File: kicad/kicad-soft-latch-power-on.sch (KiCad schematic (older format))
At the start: 9 parts, among them J1 Conn_01x03, J2 Conn_01x03, Q1 SI9942DY, SW1 SW_Push

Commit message: pcb update
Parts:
- added V?: VDC, symbol Simulation_SPICE:VDC
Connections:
- net GND: now also V?.2
- net V_IN: now also V?.1
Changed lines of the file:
@@
 Wire Wire Line
 	6900 3300 7100 3300
+Text GLabel 4550 2550 1    50   Input ~ 0
+V_IN
+$Comp
+L Simulation_SPICE:VDC V?
+U 1 1 61A0B573
+P 4550 2800
+F 0 "V?" H 4680 2891 50  0000 L CNN
+F 1 "VDC" H 4680 2800 50  0000 L CNN
+F 2 "" H 4550 2800 50  0001 C CNN
+F 3 "~" H 4550 2800 50  0001 C CNN
+F 4 "Y" H 4550 2800 50  0001 L CNN "Spice_Netlist_Enabled"
+F 5 "V" H 4550 2800 50  0001 L CNN "Spice_Primitive"
+F 6 "dc(1)" H 4680 2709 50  0000 L CNN "Spice_Model"
+	1    4550 2800
+	1    0    0    -1
+$EndComp
+Wire Wire Line
+	4550 2550 4550 2600
+$Comp
+L power:GND #PWR?
+U 1 1 61A0D8FF
+P 4550 3050
+F 0 "#PWR?" H 4550 2800 50  0001 C CNN
+F 1 "GND" H 4700 3050 50  0000 C CNN
+F 2 "" H 4550 3050 50  0001 C CNN
+F 3 "" H 4550 3050 50  0001 C CNN
+	1    4550 3050
+	1    0    0    -1
+$EndComp
+Wire Wire Line
+	4550 3050 4550 3000
 $EndSCHEMATC

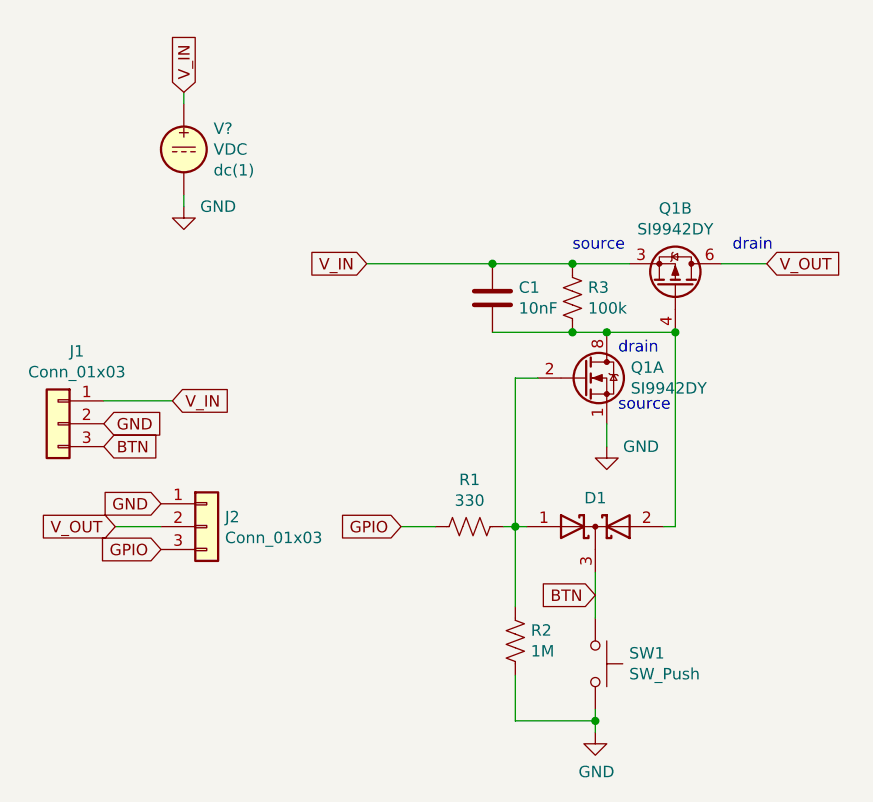
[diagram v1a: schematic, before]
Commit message: add reverse polarity protection
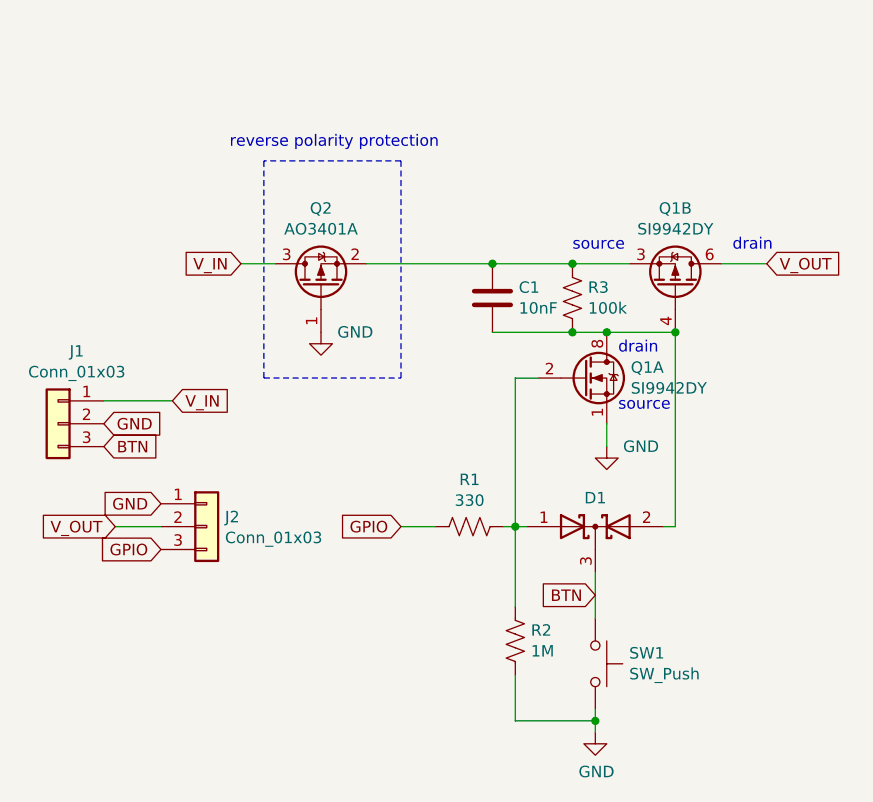
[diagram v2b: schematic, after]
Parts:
- removed V?: VDC, symbol Simulation_SPICE:VDC
- added Q2: AO3401A, Package_TO_SOT_SMD:SOT-23, symbol Transistor_FET:AO3401A
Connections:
- net GND: now also Q2.1 (G)
- net V_IN: now also Q2.3 (D); no longer C1.1, Q1.3 (1), R3.1
- new net: C1.1, Q1.3 (1), Q2.2 (S), R3.1
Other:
- note added: "reverse polarity protection"
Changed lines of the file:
@@
 Text GLabel 7100 3300 2    50   Input ~ 0
 V_OUT
-Text GLabel 5350 3300 0    50   Input ~ 0
+Text GLabel 4800 3300 0    50   Input ~ 0
 V_IN
 Wire Wire Line
@@
 Wire Wire Line
 	6900 3300 7100 3300
-Text GLabel 4550 2550 1    50   Input ~ 0
-V_IN
 $Comp
-L Simulation_SPICE:VDC V?
-U 1 1 61A0B573
-P 4550 2800
-F 0 "V?" H 4680 2891 50  0000 L CNN
-F 1 "VDC" H 4680 2800 50  0000 L CNN
-F 2 "" H 4550 2800 50  0001 C CNN
-F 3 "~" H 4550 2800 50  0001 C CNN
-F 4 "Y" H 4550 2800 50  0001 L CNN "Spice_Netlist_Enabled"
-F 5 "V" H 4550 2800 50  0001 L CNN "Spice_Primitive"
-F 6 "dc(1)" H 4680 2709 50  0000 L CNN "Spice_Model"
-	1    4550 2800
+L Transistor_FET:AO3401A Q2
+U 1 1 61A98F12
+P 5150 3400
+F 0 "Q2" V 5492 3400 50  0000 C CNN
+F 1 "AO3401A" V 5401 3400 50  0000 C CNN
+F 2 "Package_TO_SOT_SMD:SOT-23" H 5350 3325 50  0001 L CIN
+F 3 "http://www.aosmd.com/pdfs/datasheet/AO3401A.pdf" H 5150 3400 50  0001 L CNN
+	1    5150 3400
+	0    -1   -1   0
+$EndComp
+$Comp
+L power:GND #PWR04
+U 1 1 61A9DB9F
+P 5150 3600
+F 0 "#PWR04" H 5150 3350 50  0001 C CNN
+F 1 "GND" H 5300 3600 50  0000 C CNN
+F 2 "" H 5150 3600 50  0001 C CNN
+F 3 "" H 5150 3600 50  0001 C CNN
+	1    5150 3600
 	1    0    0    -1
 $EndComp
 Wire Wire Line
-	4550 2550 4550 2600
-$Comp
-L power:GND #PWR?
-U 1 1 61A0D8FF
-P 4550 3050
-F 0 "#PWR?" H 4550 2800 50  0001 C CNN
-F 1 "GND" H 4700 3050 50  0000 C CNN
-F 2 "" H 4550 3050 50  0001 C CNN
-F 3 "" H 4550 3050 50  0001 C CNN
-	1    4550 3050
-	1    0    0    -1
-$EndComp
-Wire Wire Line
-	4550 3050 4550 3000
+	4950 3300 4800 3300
+Wire Notes Line
+	4900 2850 4900 3800
+Wire Notes Line
+	4900 3800 5500 3800
+Wire Notes Line
+	5500 3800 5500 2850
+Wire Notes Line
+	5500 2850 4900 2850
+Text Notes 4750 2800 0    50   ~ 0
+reverse polarity protection
 $EndSCHEMATC

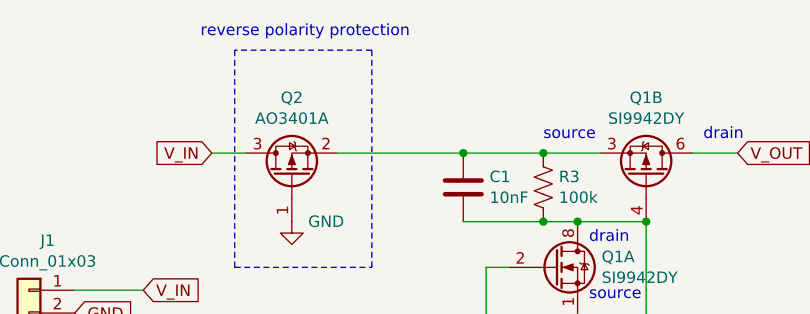
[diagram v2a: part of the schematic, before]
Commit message: final version with TH parts
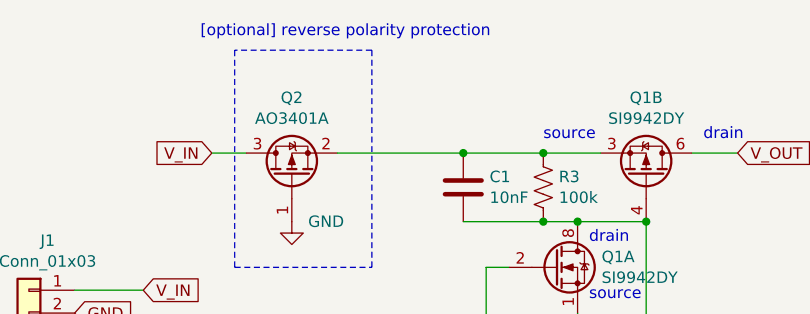
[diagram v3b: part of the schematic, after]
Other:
- note added: "[optional] reverse polarity protection"
- note removed: "reverse polarity protection"
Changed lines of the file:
@@
 	5500 2850 4900 2850
 Text Notes 4750 2800 0    50   ~ 0
-reverse polarity protection
+[optional] reverse polarity protection
 $EndSCHEMATC
